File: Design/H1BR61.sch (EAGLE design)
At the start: 24 parts, among them P1 HEXABIT_17.32_NO_P6_P7_P12, U1 STM32G0B1CEU6NUFQFPN48_STM32_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, X1 8MH

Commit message: Correcting Schematic file
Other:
- note added: "H1B6R1_Backend"
- note removed: "H1B6R1_Frontend"
- note removed: "H1BR60"
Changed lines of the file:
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@@
 <text x="215.9" y="5.3848" size="1.9304" layer="100" font="vector">Sheet   of</text>
 <text x="199.4662" y="19.6342" size="1.9304" layer="100" font="vector">Title</text>
-<text x="180.9242" y="19.6342" size="1.9304" layer="102" font="vector">H1BR60</text>
+<text x="180.9242" y="19.6342" size="1.9304" layer="102" font="vector">H1BR61</text>
 <text x="179.2478" y="11.2014" size="1.9304" layer="101" font="vector">Micro SD Card Reader</text>
-<text x="205.53045" y="19.79295" size="1.9304" layer="101" font="vector">H1B6R1_Frontend</text>
+<text x="205.53045" y="19.79295" size="1.9304" layer="101" font="vector">H1B6R1_Backend</text>
 <wire x1="168.91" y1="3.81" x2="168.91" y2="8.128" width="0.1524" layer="205"/>
 <wire x1="168.91" y1="8.128" x2="168.91" y2="18.288" width="0.1524" layer="205"/>

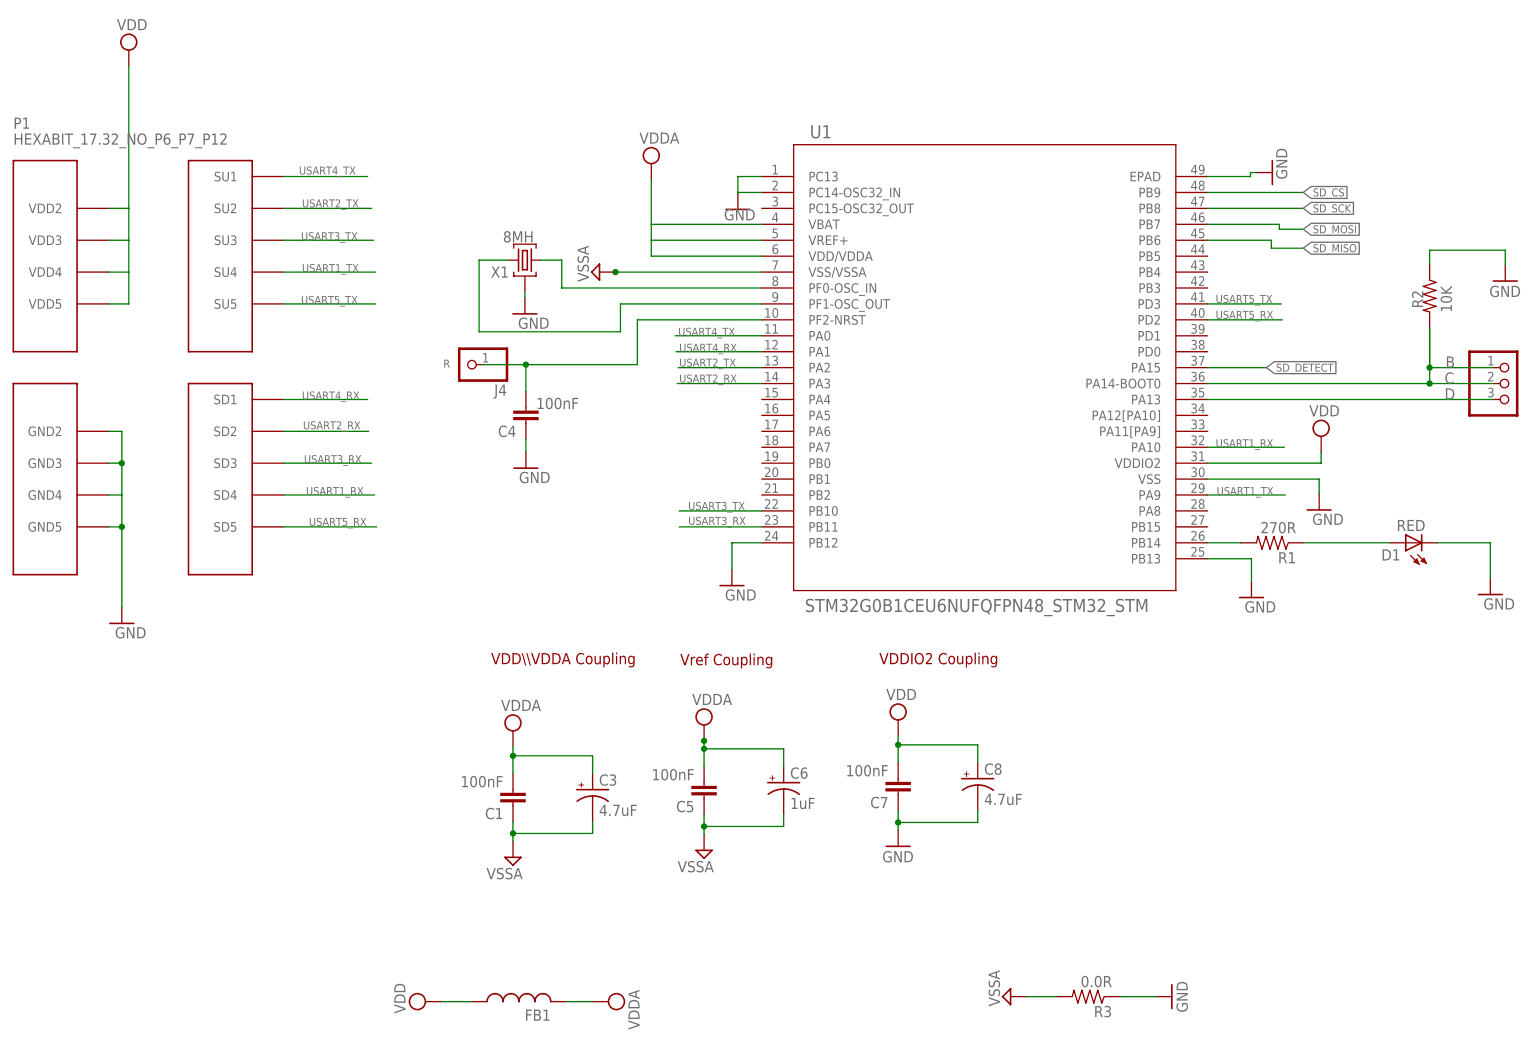
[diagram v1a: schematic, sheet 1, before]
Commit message: -Correcting some documentaion issues
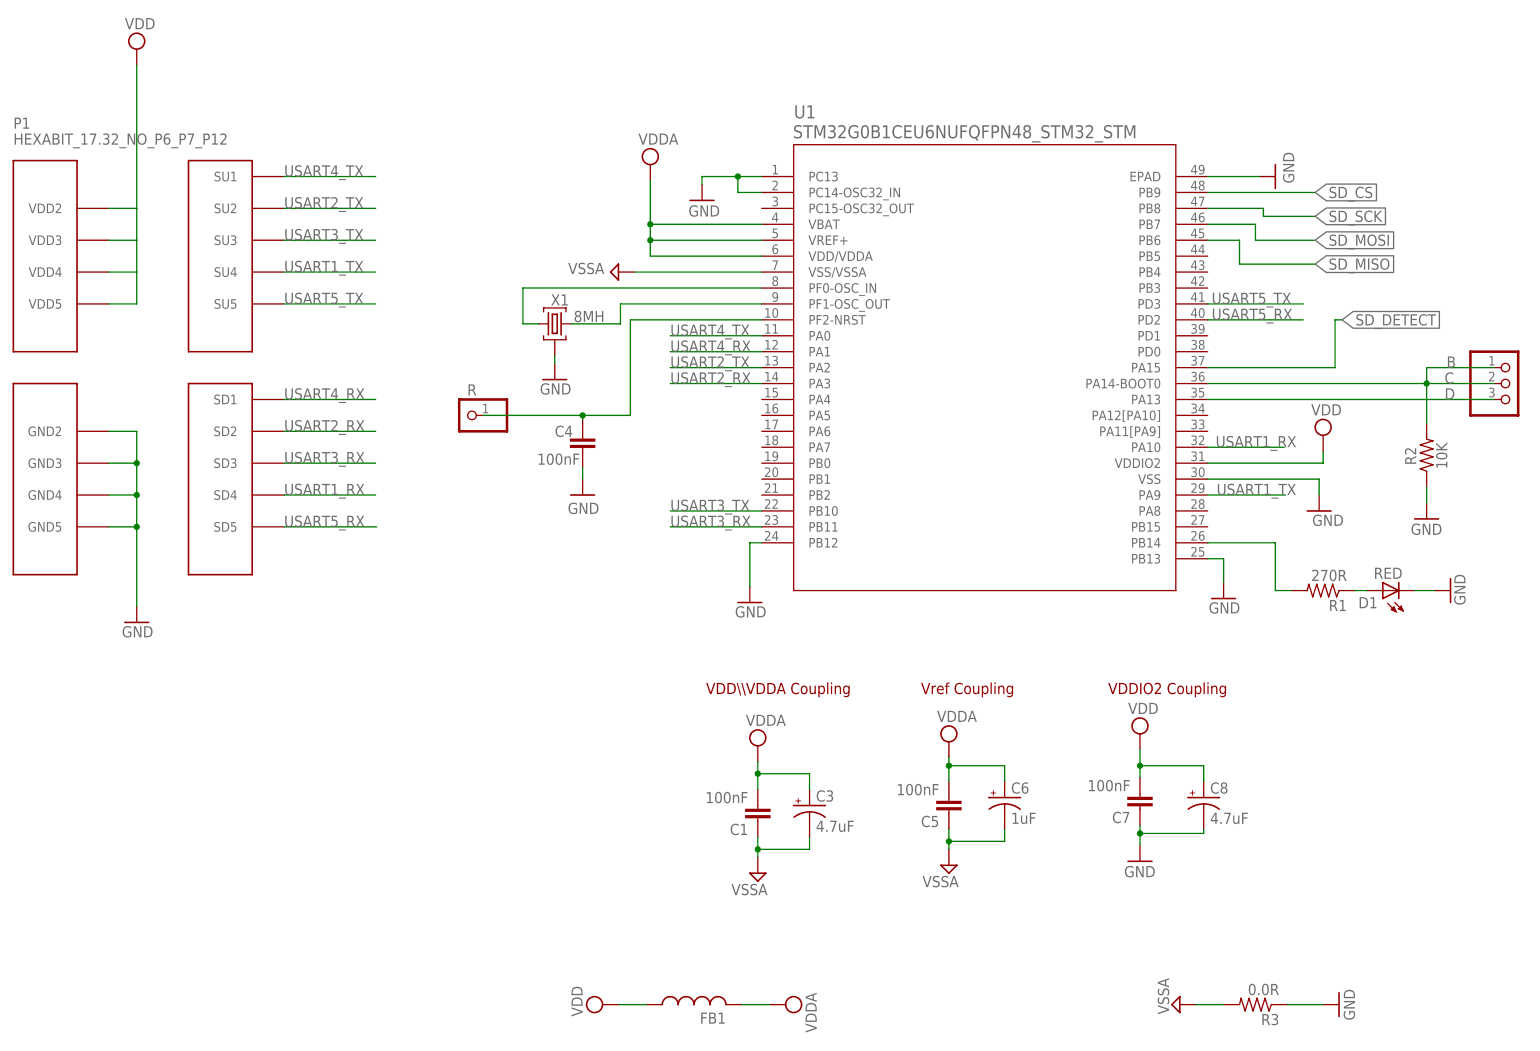
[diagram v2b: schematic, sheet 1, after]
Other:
- note added: "R"
- note added: "SPI2"
- moved on the sheet: C1, C3, C4, C5, C6, C7, C8, C9, D1, FB1, R1, R2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
